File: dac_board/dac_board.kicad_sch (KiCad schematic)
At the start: 1 part, among them J1 AudioJack3_Ground

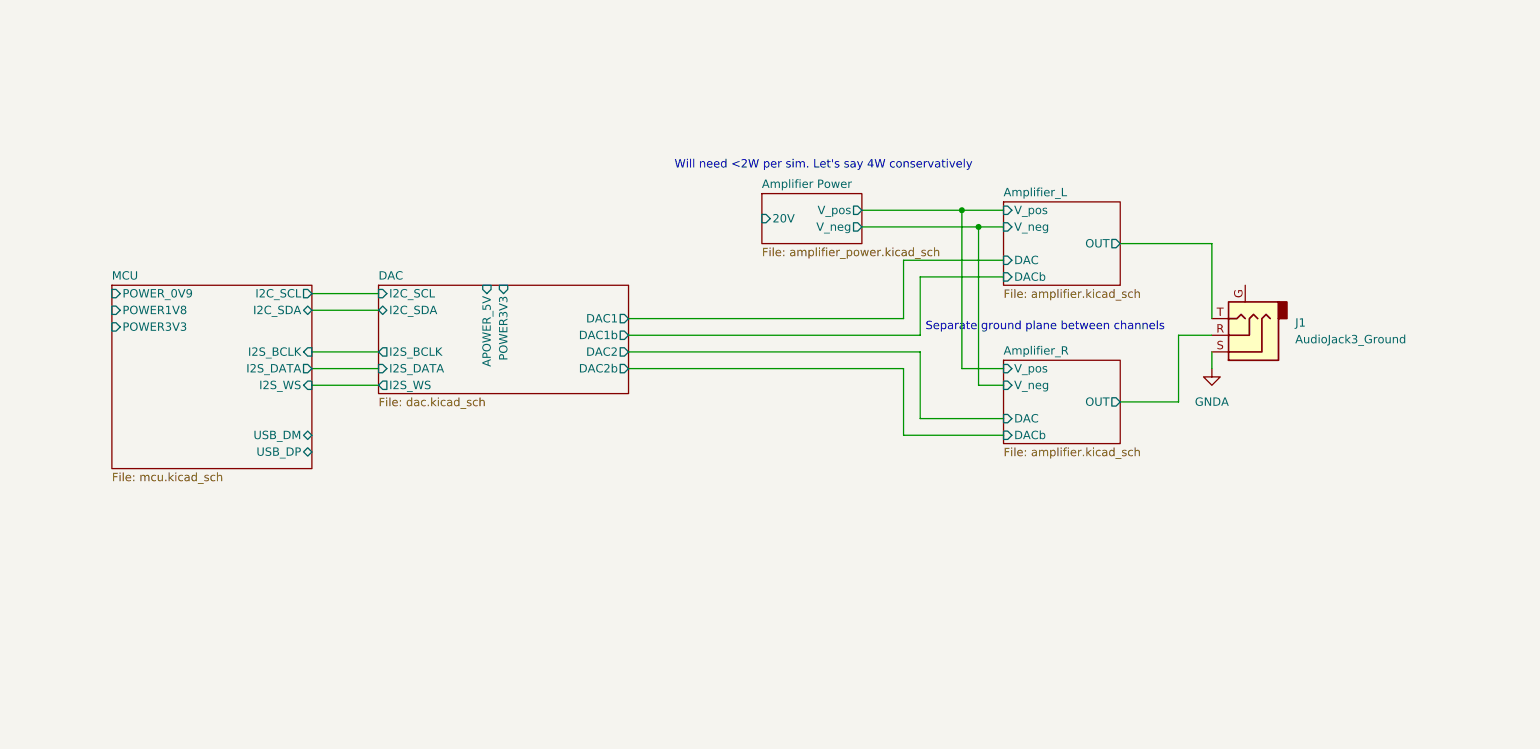
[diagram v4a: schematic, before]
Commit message: Updated schematic with detailed info from SPICE simulations
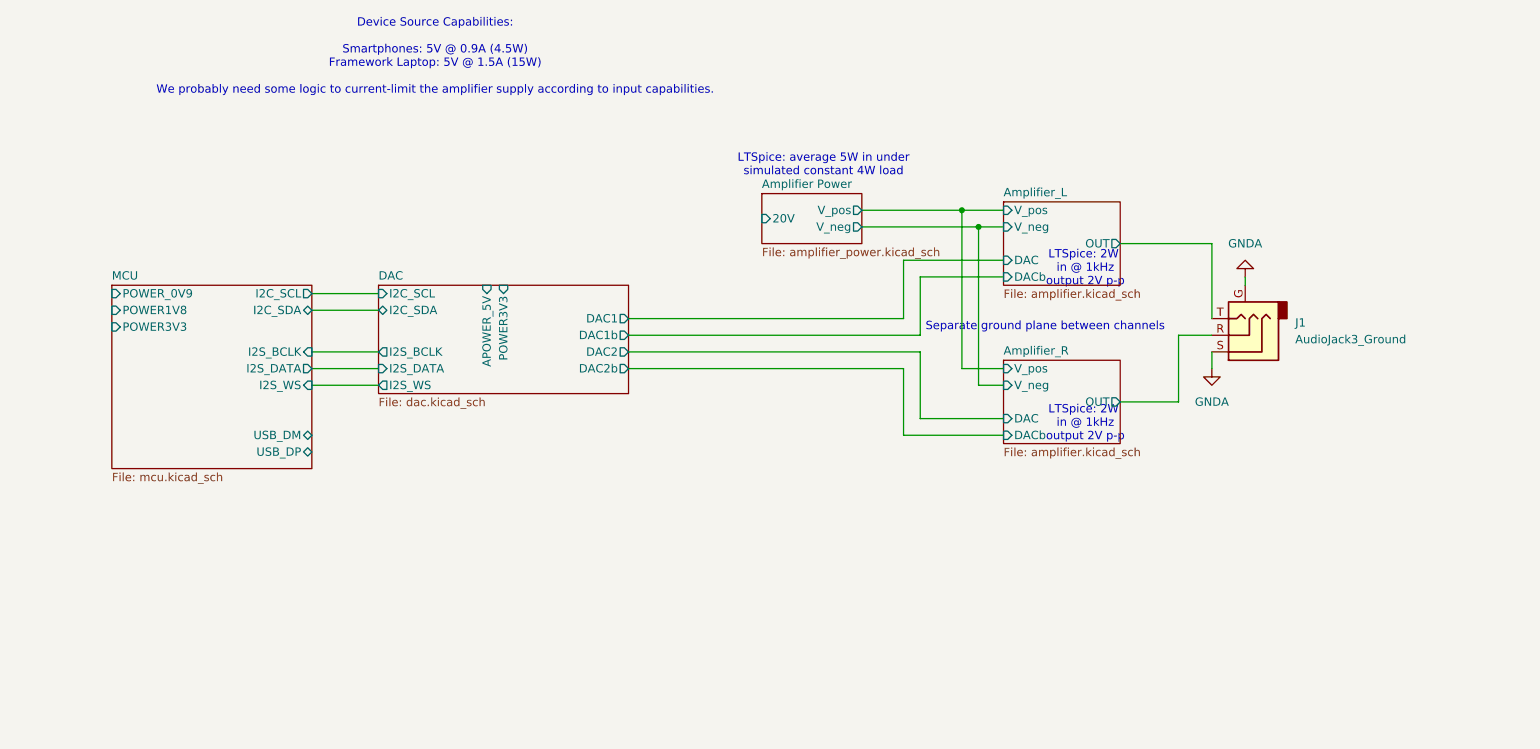
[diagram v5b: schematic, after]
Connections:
- net GNDA: now also J1.G
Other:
- note added: "Device Source Capabilities: Smartphones: 5V @ 0.9A (4.5W) Framework Laptop: 5V @ 1.5A (15W) We probably need some logic to current-limit the amplifier supply according to input capabilities."
- note added: "LTSpice: 2W in @ 1kHz output 2V p-p"
- note added: "LTSpice: average 5W in under simulated constant 4W load"
- note removed: "Will need <2W per sim. Let's say 4W conservatively"
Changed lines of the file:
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@@
 	(generator_version "9.0")
 	(paper "A4")
-	(text "Will need <2W per sim. Let's say 4W conservatively"
+	(text "LTSpice: 2W\n in @ 1kHz\n output 2V p-p"
+		(exclude_from_sim no)
+		(at 210.312 82.55 0)
+		(effects
+			(font
+				(size 1.27 1.27)
+			)
+		)
+	)
+	(text "LTSpice: average 5W in under\nsimulated constant 4W load"
 		(exclude_from_sim no)
 		(at 170.688 66.802 0)
@@
 		)
 	)
+	(text "Device Source Capabilities:\n\nSmartphones: 5V @ 0.9A (4.5W)\nFramework Laptop: 5V @ 1.5A (15W)\n\nWe probably need some logic to current-limit the amplifier supply according to input capabilities."
+		(exclude_from_sim no)
+		(at 111.506 50.292 0)
+		(effects
+			(font
+				(size 1.27 1.27)
+			)
+		)
+	)
+	(text "LTSpice: 2W\n in @ 1kHz\n output 2V p-p"
+		(exclude_from_sim no)
+		(at 210.312 106.172 0)
+		(effects
+			(font
+				(size 1.27 1.27)
+			)
+		)
+	)
 	(junction
 		(at 191.77 73.66)
@@
 		(pts
 			(xy 176.53 76.2) (xy 194.31 76.2)
+		)
+		(stroke
+			(width 0)
+			(type default)
+		)
+	)
+	(wire
+		(pts
+			(xy 234.95 83.82) (xy 234.95 85.09)
 		)
 		(stroke
@@
 					(unit 1)
 				)
+			)
+		)
+	)
+	(symbol
+		(lib_id "power:GNDA")
+		(at 234.95 83.82 180)
+		(unit 1)
+		(exclude_from_sim no)
+		(in_bom yes)
+		(on_board yes)
+		(dnp no)
+		(fields_autoplaced yes)
+		(property "Reference" "#PWR057"
+			(at 234.95 77.47 0)
+			(effects
+				(font
+					(size 1.27 1.27)
+				)
+				(hide yes)
+			)
+		)
+		(property "Value" "GNDA"
+			(at 234.95 78.74 0)
+			(effects
+				(font
+					(size 1.27 1.27)
+				)
+			)
+		)
+		(property "Footprint" ""
+			(at 234.95 83.82 0)
+			(effects
+				(font
+					(size 1.27 1.27)
+				)
+				(hide yes)
+			)
+		)
+		(property "Datasheet" ""
+			(at 234.95 83.82 0)
+			(effects
+				(font
+					(size 1.27 1.27)
+				)
+				(hide yes)
+			)
+		)
+		(property "Description" "Power symbol creates a global label with name \"GNDA\" , analog ground"
+			(at 234.95 83.82 0)
+			(effects
+				(font
+					(size 1.27 1.27)
+				)
+				(hide yes)
+			)
+		)
+		(pin "1"
+		)
+		(instances
+			(project ""
+				(path "/387b6079-e547-4b62-84b5-51a54c04db0a"
+					(reference "#PWR057")
+					(unit 1)
+				)

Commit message: More SPICE updates
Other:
- note added: "Amplifier LTSpice: 2W for 4V p-p 4W for 10V p-p @ 1kHz"
- note added: "Amplifier Power LTSpice: average 5W in under simulated constant 4W load average 8.5W in under simulated constant 8W load"
- note removed: "LTSpice: 2W in @ 1kHz output 2V p-p"
- note removed: "LTSpice: average 5W in under simulated constant 4W load"
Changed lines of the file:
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@@
 	(generator_version "9.0")
 	(paper "A4")
-	(text "LTSpice: 2W\n in @ 1kHz\n output 2V p-p"
+	(text "Amplifier LTSpice:\n2W for 4V p-p\n4W for 10V p-p\n @ 1kHz"
 		(exclude_from_sim no)
-		(at 210.312 82.55 0)
+		(at 197.104 64.77 0)
 		(effects
 			(font
 				(size 1.27 1.27)
 			)
+			(justify left)
 		)
 	)
-	(text "LTSpice: average 5W in under\nsimulated constant 4W load"
+	(text "Amplifier Power LTSpice:\naverage 5W in under simulated constant 4W load\naverage 8.5W in under simulated constant 8W load"
 		(exclude_from_sim no)
-		(at 170.688 66.802 0)
+		(at 170.18 62.738 0)
 		(effects
 			(font
@@
 		(effects
 			(font
-				(size 1.27 1.27)
-			)
-		)
-	)
-	(text "LTSpice: 2W\n in @ 1kHz\n output 2V p-p"
-		(exclude_from_sim no)
-		(at 210.312 106.172 0)
-		(effects
-			(font

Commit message: Power stuff
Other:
- note added: "Amplifier LTSpice: 2W for 4V p-p 4W for 10V p-p More than that would require additional last-stage opamp circuits @ 1kHz"
- note removed: "Amplifier LTSpice: 2W for 4V p-p 4W for 10V p-p @ 1kHz"
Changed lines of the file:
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@@
 	(generator_version "9.0")
 	(paper "A4")
-	(text "Amplifier LTSpice:\n2W for 4V p-p\n4W for 10V p-p\n @ 1kHz"
+	(text "Amplifier LTSpice:\n2W for 4V p-p\n4W for 10V p-p\nMore than that would require additional last-stage opamp circuits\n @ 1kHz"
 		(exclude_from_sim no)
-		(at 197.104 64.77 0)
+		(at 197.866 64.262 0)
 		(effects
 			(font

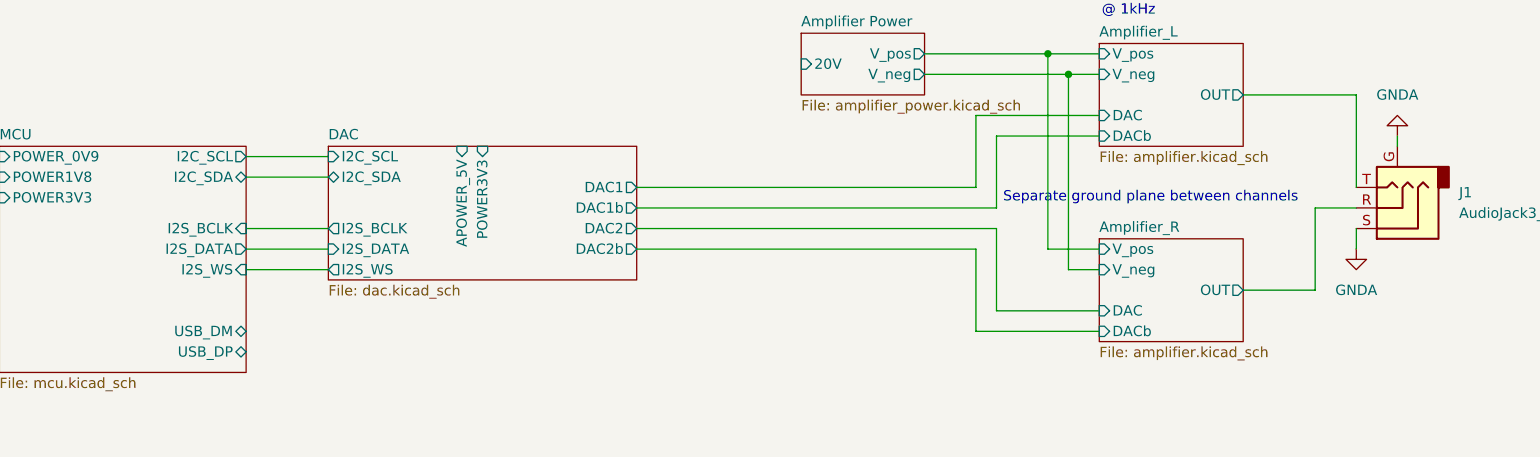
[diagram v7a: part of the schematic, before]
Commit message: Finished schematic design for MCU + DAC
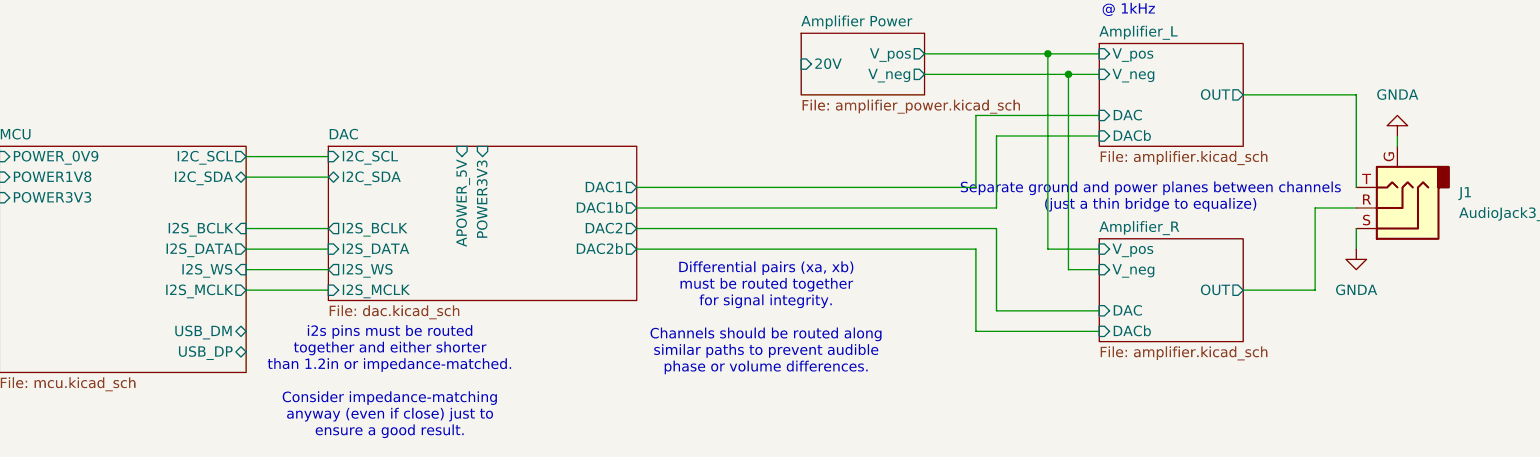
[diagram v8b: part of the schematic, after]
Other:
- sheet DAC ports: added I2S_MCLK; removed none
- sheet MCU ports: added I2S_MCLK; removed none
- note added: "Differential pairs (xa, xb) must be routed together for signal integrity. Channels should be routed along similar paths to prevent audible phase or volume differences."
- note added: "Separate ground and power planes between channels (just a thin bridge to equalize)"
- note added: "i2s pins must be routed together and either shorter than 1.2in or impedance-matched. Consider impedance-matching anyway (even if close) just to ensure a good result."
- note removed: "Separate ground plane between channels"
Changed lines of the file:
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@@
 		)
 	)
-	(text "Separate ground plane between channels"
+	(text "Separate ground and power planes between channels\n(just a thin bridge to equalize)"
 		(exclude_from_sim no)
 		(at 204.47 91.44 0)
+		(effects
+			(font
+				(size 1.27 1.27)
+			)
+		)
+	)
+	(text "Differential pairs (xa, xb)\nmust be routed together\nfor signal integrity.\n\nChannels should be routed along\nsimilar paths to prevent audible\nphase or volume differences."
+		(exclude_from_sim no)
+		(at 156.972 106.426 0)
 		(effects
 			(font
@@
 		)
 	)
+	(text "i2s pins must be routed\ntogether and either shorter\nthan 1.2in or impedance-matched.\n\nConsider impedance-matching\nanyway (even if close) just to\nensure a good result."
+		(exclude_from_sim no)
+		(at 110.49 114.3 0)
+		(effects
+			(font
+				(size 1.27 1.27)
+			)
+		)
+	)
 	(junction
 		(at 191.77 73.66)
@@
 		(pts
 			(xy 185.42 105.41) (xy 198.12 105.41)
+		)
+		(stroke
+			(width 0)
+			(type default)
+		)
+	)
+	(wire
+		(pts
+			(xy 92.71 102.87) (xy 102.87 102.87)
 		)
 		(stroke
@@
 			)
 		)
+		(pin "I2S_MCLK" output
+			(at 92.71 102.87 0)
+			(effects
+				(font
+					(size 1.27 1.27)
+				)
+				(justify right)
+			)
+		)
 		(instances
 			(project "dac_board"
@@
 	(sheet
 		(at 102.87 85.09)
-		(size 38.1 16.51)
+		(size 38.1 19.05)
 		(exclude_from_sim no)
 		(in_bom yes)
@@
 		)
 		(property "Sheetfile" "dac.kicad_sch"
-			(at 102.87 102.1846 0)
+			(at 102.87 104.7246 0)
 			(effects
 				(font
@@
 			)
 		)
+		(pin "I2S_MCLK" input
+			(at 102.87 102.87 180)
+			(effects
+				(font
+					(size 1.27 1.27)
+				)
+				(justify left)
+			)
+		)
